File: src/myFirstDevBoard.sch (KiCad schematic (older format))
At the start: 36 parts, among them J1 Conn_01x15_Male, J2 Conn_01x15_Male, Q1 BC550, Q2 BC550, Q3 BC550, SW1 SW_Push, SW2 SW_Push, SW3 SW_Push, SW4 SW_Push, SW5 SW_SLIDER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

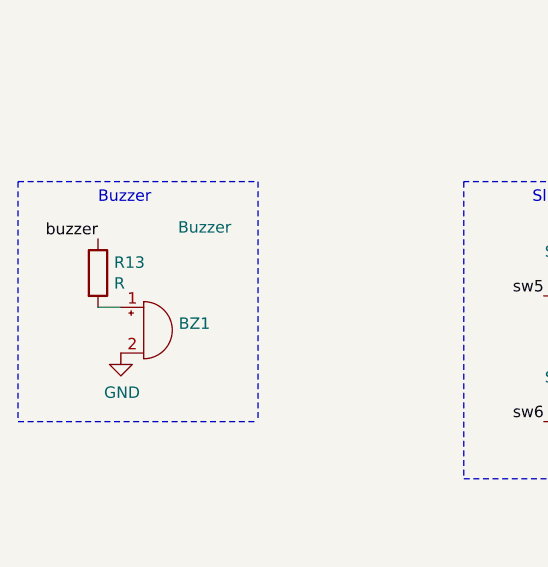
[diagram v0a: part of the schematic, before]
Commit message: adding buzzer resistor
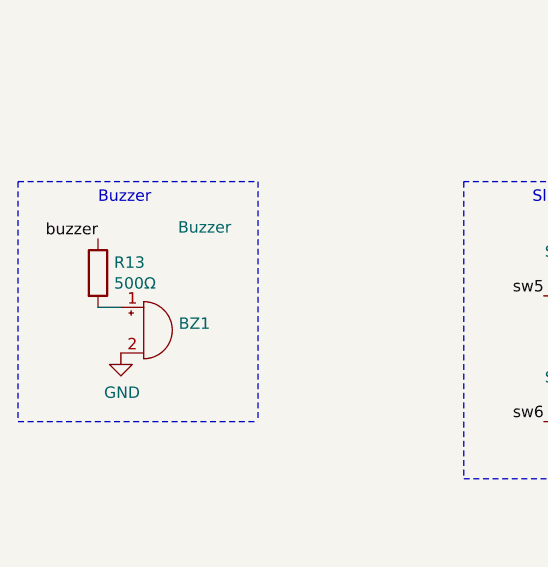
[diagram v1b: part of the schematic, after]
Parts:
- R13: value R -> 500Ω
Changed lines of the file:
@@
 P 1100 4500
 F 0 "R13" H 1170 4546 50  0000 L CNN
-F 1 "R" H 1170 4455 50  0000 L CNN
+F 1 "500Ω" H 1170 4455 50  0000 L CNN
 F 2 "lib:R_Axial_DIN0207_L6.3mm_D2.5mm_P10.16mm_Horizontal_oval" V 1030 4500 50  0001 C CNN
 F 3 "~" H 1100 4500 50  0001 C CNN

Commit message: prepping for schematic deployment
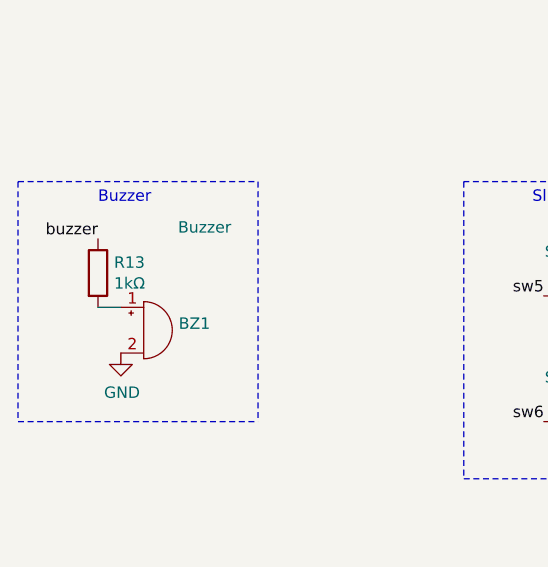
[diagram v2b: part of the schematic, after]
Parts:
- R13: value 500Ω -> 1kΩ
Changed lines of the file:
@@
 EESchema Schematic File Version 4
 LIBS:myFirstDevBoard-cache
-EELAYER 26 0
+EELAYER 29 0
 EELAYER END
 $Descr A4 11693 8268
@@
 P 1100 4500
 F 0 "R13" H 1170 4546 50  0000 L CNN
-F 1 "500Ω" H 1170 4455 50  0000 L CNN
+F 1 "1kΩ" H 1170 4455 50  0000 L CNN
 F 2 "lib:R_Axial_DIN0207_L6.3mm_D2.5mm_P10.16mm_Horizontal_oval" V 1030 4500 50  0001 C CNN
 F 3 "~" H 1100 4500 50  0001 C CNN
